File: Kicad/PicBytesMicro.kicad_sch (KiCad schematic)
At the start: 9 parts

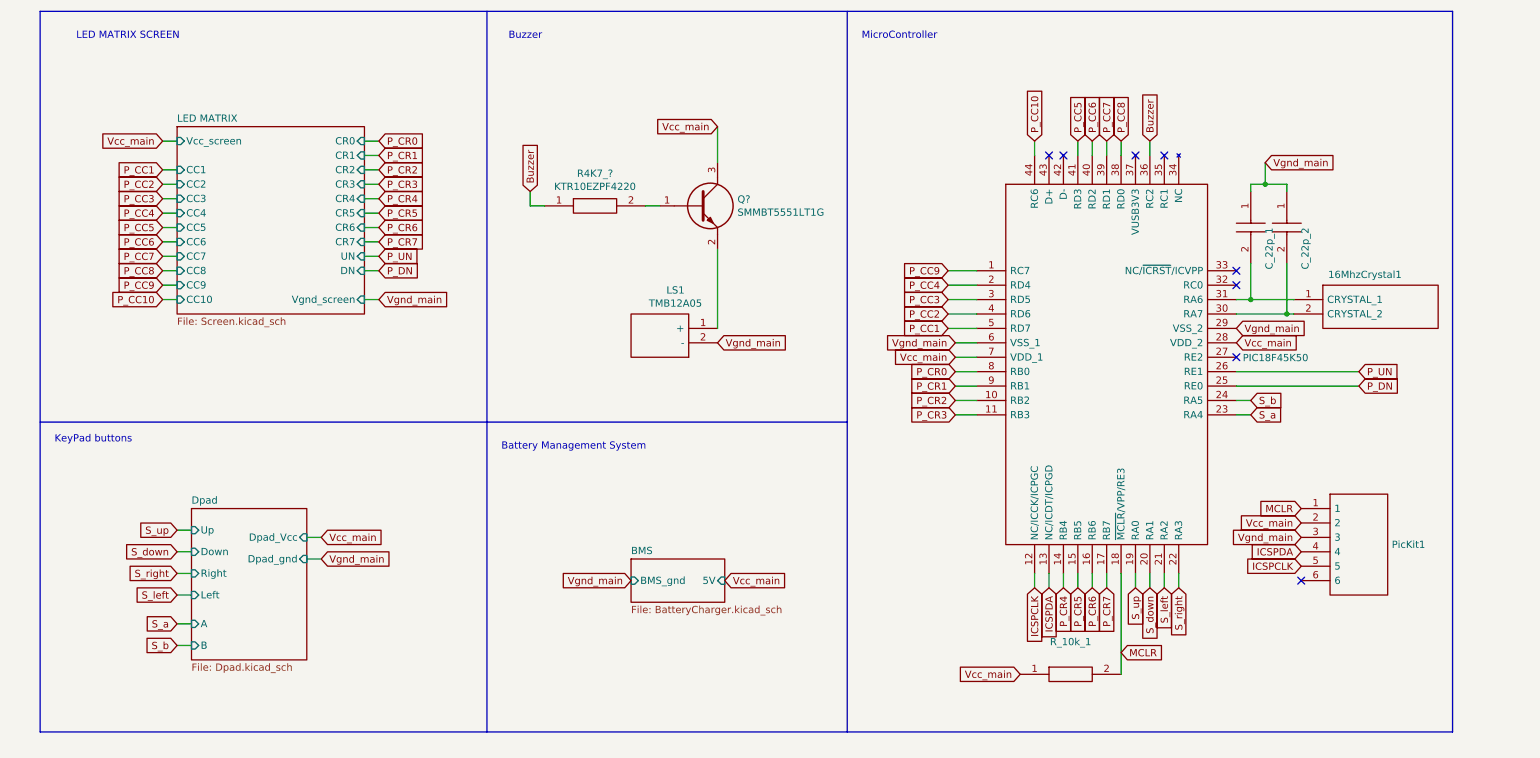
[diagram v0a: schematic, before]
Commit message: New V1.2 Hardware Release
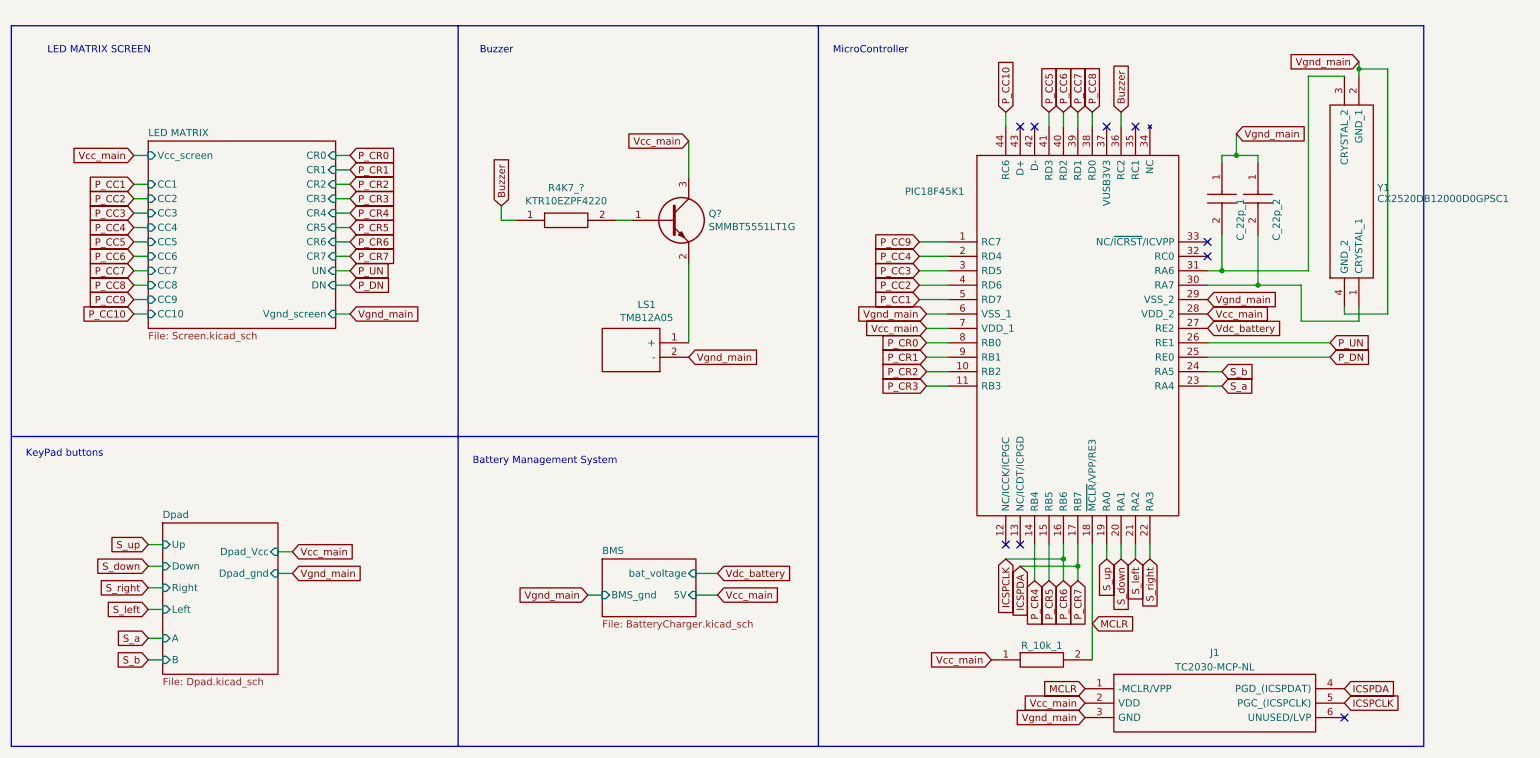
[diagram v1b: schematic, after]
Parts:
- removed 16MhzCrystal1: AS-16.000MAHK-B, AS16000MAHKB, symbol PicBytesMicro-rescue:AS-16.000MAHK-B-SamacSys_Parts
- removed PicKit1: M20-9990645, HDRV6W66P0X254_1X6_1524X254X874P, symbol PicBytesMicro-rescue:M20-9990645-SamacSys_Parts
- added J1: TC2030-MCP-NL, TC2030-MCP-NL, symbol User_lib:TC2030-MCP-NL
- added Y1: CX2520DB12000D0GPSC1, CX2520DB12000D0GPSC1, symbol User_lib:CX2520DB12000D0GPSC1
- renumbered PIC18F45K50 to PIC18F45K1
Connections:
- net P_CR6 is gone; now on net ICSPCLK: PIC18F45K1.16 (RB6)
- net P_CR7 is gone; now on net ICSPDA: PIC18F45K1.17 (RB7)
- net ICSPCLK: now also J1.5 (PGC_(ICSPCLK)); no longer PIC18F45K1.12 (NC/ICCK/ICPGC)
- net ICSPDA: now also J1.4 (PGD_(ICSPDAT)); no longer PIC18F45K1.13 (NC/ICDT/ICPGD)
- net MCLR: now also J1.1 (-MCLR/VPP)
- net Vcc_main: now also J1.2 (VDD)
- net Vgnd_main: now also J1.3 (GND), Y1.2 (GND_1), Y1.4 (GND_2)
- net at C_22p_1.2, PIC18F45K1.31 (RA6): now also Y1.3 (CRYSTAL_2)
- net at C_22p_2.2, PIC18F45K1.30 (RA7): now also Y1.1 (CRYSTAL_1)
- net Vdc_battery: now reaches PIC18F45K1.27 (RE2)
- no-connect marks 8 -> 9
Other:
- sheet BMS ports: added bat_voltage; removed none
- moved on the sheet: C_22p_1, C_22p_2, LS1, PIC18F45K1, Q?, R4K7_?, R_10k_1
